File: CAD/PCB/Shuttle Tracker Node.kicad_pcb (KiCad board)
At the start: 2 copper layers, 105.2 x 45.7 mm, 27 parts, among them J1 Conn_01x01, J2 Conn_01x01, J3 Conn_01x01, J4 Conn_01x01, J5 Conn_01x01, J6 Conn_01x01, J7 Conn_01x01, SW1 SW_Push, SW10 SW_Push, SW11 SW_Push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

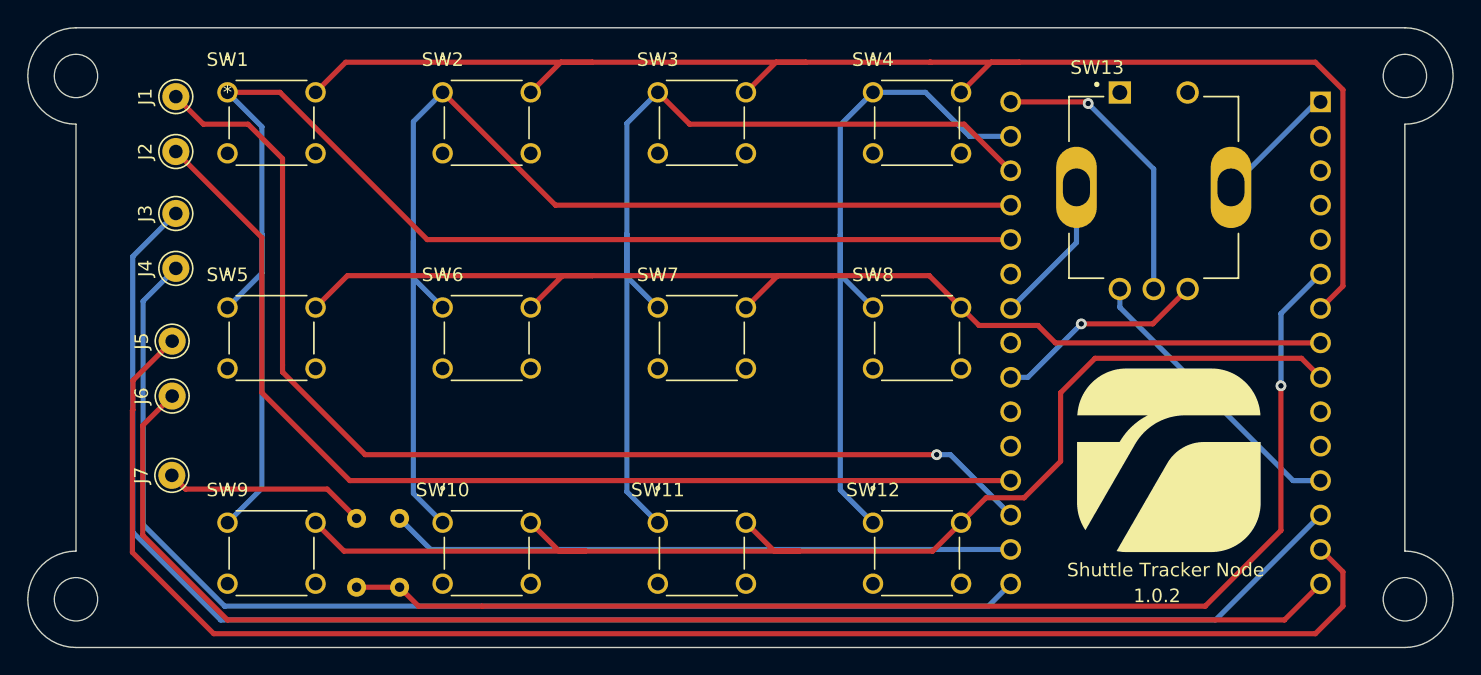
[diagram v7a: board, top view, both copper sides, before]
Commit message: Changed location of mounting holes
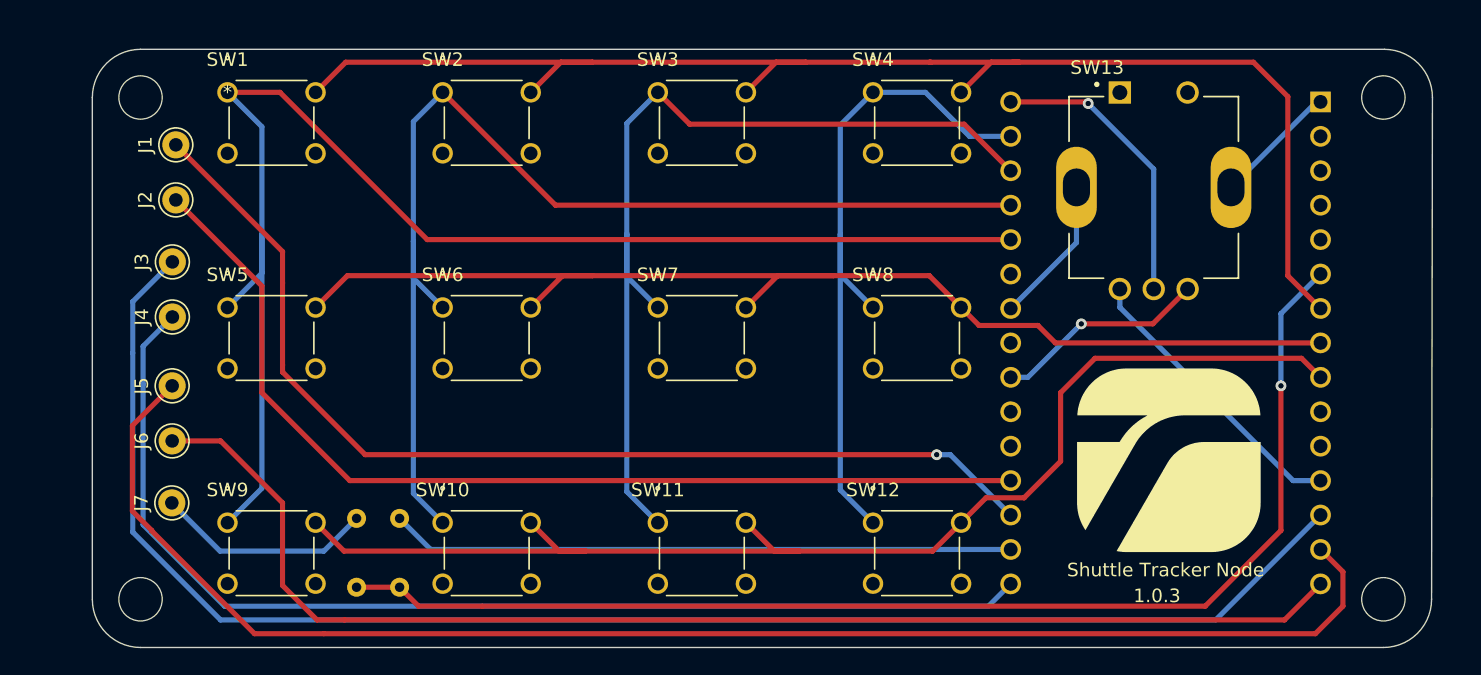
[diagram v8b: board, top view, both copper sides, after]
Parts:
- moved REF** 5.02 mm to (133.3, 81.3)
- moved REF** 4.76 mm to (133.3, 118.4)
- moved J4 3.59 mm to (135.6, 97.5)
- moved J3 3.58 mm to (135.6, 93.5)
- moved J2 3.57 mm to (135.9, 88.9)
- moved J1 3.56 mm to (135.9, 84.8)
- moved J6 3.31 mm to (135.6, 106.7)
- moved J5 3.30 mm to (135.6, 102.6)
- moved REF** 2.25 mm to (225.0, 81.3)
- moved J7 2.03 mm to (135.6, 111.3)
- moved REF** 1.59 mm to (225.0, 118.4)
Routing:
- net BAT_GND: track 101.8 -> 94.9 mm
- net LCD_DAT: track 83.6 -> 78.1 mm
- net BAT_5V: track 114.3 -> 109.2 mm
- net LCD_GND: track 87.1 -> 83.4 mm
- net LCD_5V: track 118.3 -> 114.7 mm
- net LCD_CLK: track 78.4 -> 74.8 mm
- net R1: track 110.5 -> 107.0 mm
- net V_IN: track 14.9 -> 16.1 mm
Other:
- board size 105.2 x 45.7 mm -> 98.9 x 44.1 mm
- board text added: "1.0.3"
- board text removed: "1.0.2"
